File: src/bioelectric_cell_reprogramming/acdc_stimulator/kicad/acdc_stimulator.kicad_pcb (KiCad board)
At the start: 4 copper layers, 0 parts

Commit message: ci: STM32 layout done and schematic annotated
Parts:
- added C1: 100n, Capacitor_SMD:C_0402_1005Metric, F.Cu at (104.7, 48.6)
- added C10: 100n, Capacitor_SMD:C_0402_1005Metric, F.Cu at (112.9, 57.5)
- added C11: 30p, Capacitor_SMD:C_0402_1005Metric, F.Cu at (118.8, 55.8)
- added C12: 100n, Capacitor_SMD:C_0402_1005Metric, F.Cu at (112.4, 53.6)
- added C13: 100n, Capacitor_SMD:C_0402_1005Metric, F.Cu at (100.8, 48.6)
- added C14: 100n, Capacitor_SMD:C_0402_1005Metric, F.Cu at (97.6, 60.1)
- added C15: 100n, Capacitor_SMD:C_0402_1005Metric, F.Cu at (108.2, 64.2)
- added C16: 22u, Capacitor_SMD:C_0805_2012Metric, F.Cu at (223.9, 36.3)
- added C17: 10n, Capacitor_SMD:C_0402_1005Metric, F.Cu at (102.7, 48.6)
- added C18: 22u, Capacitor_SMD:C_0805_2012Metric, F.Cu at (223.9, 39.4)
- added C19: 1u, Capacitor_SMD:C_0402_1005Metric, F.Cu at (102.8, 45.3)
- added C2: 100n, Capacitor_SMD:C_0402_1005Metric, F.Cu at (196.5, 37.8)
- added C20: 1u, Capacitor_SMD:C_0402_1005Metric, F.Cu at (102.8, 43.7)
- added C21: 0.1u, Capacitor_SMD:C_0402_1005Metric, F.Cu at (196.5, 41.7)
- added C22: 10u, Capacitor_SMD:C_0603_1608Metric, F.Cu at (223.7, 64.5)
- added C23: 100n, Capacitor_SMD:C_0402_1005Metric, F.Cu at (202.2, 43.7)
- added C24: 100u, Capacitor_THT:C_Disc_D7.5mm_W2.5mm_P5.00mm, F.Cu at (205.7, 36.9)
- added C25: 100u, Capacitor_THT:C_Disc_D7.5mm_W2.5mm_P5.00mm, F.Cu at (205.7, 40.9)
- added C26: 0.1u, Capacitor_SMD:C_0402_1005Metric, F.Cu at (245.1, 64.4)
- added C27: 0.1u, Capacitor_SMD:C_0402_1005Metric, F.Cu at (245.1, 62.4)
- added C28: 1n, Capacitor_SMD:C_0402_1005Metric, F.Cu at (248.0, 60.4)
- added C29: 4.7u, Capacitor_SMD:C_0603_1608Metric, F.Cu at (230.8, 54.0)
- added C3: 10u, Capacitor_SMD:CP_Elec_5x5.4, F.Cu at (217.2, 38.3)
- added C30: 4.7u, Capacitor_SMD:C_0603_1608Metric, F.Cu at (230.8, 56.5)
- added C31: 4.7u, Capacitor_SMD:C_0603_1608Metric, F.Cu at (234.8, 46.5)
- added C32: 4.7u, Capacitor_SMD:C_0603_1608Metric, F.Cu at (234.8, 49.0)
- added C33: 4.7u, Capacitor_SMD:C_0603_1608Metric, F.Cu at (234.8, 51.5)
- added C34: 4.7u, Capacitor_SMD:C_0603_1608Metric, F.Cu at (234.8, 54.0)
- added C35: 4.7u, Capacitor_SMD:C_0603_1608Metric, F.Cu at (234.8, 56.5)
- added C36: 0.1u, Capacitor_SMD:C_0402_1005Metric, F.Cu at (245.1, 60.4)
- added C37: 4.7u, Capacitor_SMD:C_0603_1608Metric, F.Cu at (238.8, 46.5)
- added C38: 47u, Capacitor_THT:CP_Radial_D10.0mm_P5.00mm, F.Cu at (232.3, 63.6)
- added C39: 0.1u, Capacitor_SMD:C_0402_1005Metric, F.Cu at (242.2, 64.4)
- added C4: 100n, Capacitor_SMD:C_0402_1005Metric, F.Cu at (196.5, 39.8)
- added C40: 2.2u, Capacitor_SMD:C_0603_1608Metric, F.Cu at (230.8, 46.5)
- added C41: 100p, Capacitor_SMD:C_0402_1005Metric, F.Cu at (248.0, 62.4)
- added C42: 0.1u, Capacitor_SMD:C_0402_1005Metric, F.Cu at (242.2, 62.4)
- added C43: 2.2u, Capacitor_SMD:C_0603_1608Metric, F.Cu at (230.8, 49.0)
- added C44: 0.1u, Capacitor_SMD:C_0402_1005Metric, F.Cu at (242.2, 60.4)
- added C45: 15n, Capacitor_SMD:C_0402_1005Metric, F.Cu at (248.0, 64.4)
- added C46: 4.7u, Capacitor_SMD:C_0603_1608Metric, F.Cu at (230.8, 51.5)
- added C47: 1u, Capacitor_SMD:C_0402_1005Metric, F.Cu at (238.7, 110.6)
- added C48: 100n, Capacitor_SMD:C_0402_1005Metric, F.Cu at (238.7, 112.6)
- added C49: 100n, Capacitor_SMD:C_0402_1005Metric, F.Cu at (238.7, 118.5)
- added C5: 1u, Capacitor_SMD:C_0402_1005Metric, F.Cu at (104.7, 47.5)
- added C50: 47n, Capacitor_SMD:C_0402_1005Metric, F.Cu at (238.7, 114.6)
- added C51: 1u, Capacitor_SMD:C_0402_1005Metric, F.Cu at (238.7, 116.5)
- added C52: 10u, Capacitor_SMD:CP_Elec_5x5.4, F.Cu at (229.9, 125.3)
- added C53: 2.2u, Capacitor_SMD:C_0603_1608Metric, F.Cu at (243.9, 103.9)
- added C54: 47u, Capacitor_SMD:C_0805_2012Metric, F.Cu at (244.1, 101.1)
- added C55: 2.2u, Capacitor_SMD:C_0603_1608Metric, F.Cu at (218.3, 103.9)
- added C56: 47u, Capacitor_SMD:C_0805_2012Metric, F.Cu at (218.5, 101.1)
- added C57: 2.2u, Capacitor_SMD:C_0603_1608Metric, F.Cu at (218.3, 126.0)
- added C58: 47u, Capacitor_SMD:C_0805_2012Metric, F.Cu at (218.5, 123.2)
- added C6: 10n, Capacitor_SMD:C_0402_1005Metric, F.Cu at (196.5, 35.8)
- added C7: 30p, Capacitor_SMD:C_0402_1005Metric, F.Cu at (116.4, 60.8)
- added C8: 10u, Capacitor_SMD:C_0603_1608Metric, F.Cu at (119.7, 78.4)
- added C9: 100n, Capacitor_SMD:C_0402_1005Metric, F.Cu at (112.4, 60.0)
- added D1: LED, LED_SMD:LED_0402_1005Metric, F.Cu at (181.1, 72.2)
- added D2: MBR2100, MBR2100:DIOAD1910W86L670D310, F.Cu at (227.0, 89.0)
- added D3: MBR2100, MBR2100:DIOAD1910W86L670D310, F.Cu at (201.4, 89.0)
- added D4: MBR2100, MBR2100:DIOAD1910W86L670D310, F.Cu at (201.4, 111.1)
- added F1: 500mA, Fuse:Fuse_0603_1608Metric, F.Cu at (89.0, 50.0)
- added FB1: 120R, Inductor_SMD:L_0603_1608Metric, F.Cu at (100.9, 44.5)
- added IC1: AD9833BRM-REEL7, AD9833BRM-REEL7:SOP50P490X110-10N, F.Cu at (215.6, 82.2)
- added IC2: AD5122BCPZ10-RL7, AD5122BCPZ10-RL7:QFN50P300X300X80-17N-D, F.Cu at (224.1, 44.3)
- added IC3: LTC3896EFE#PBF, LTC3896EFE#PBF:SOP50P640X120-39N, F.Cu at (254.8, 50.9)
- added IC4: LTC3637IMSE#PBF, LTC3637IMSE#PBF:LTC3637IMSEPBF, F.Cu at (245.4, 95.5)
- added IC5: LTC3637IMSE#PBF, LTC3637IMSE#PBF:LTC3637IMSEPBF, F.Cu at (219.9, 95.5)
- added IC6: LTC3637IMSE#PBF, LTC3637IMSE#PBF:LTC3637IMSEPBF, F.Cu at (219.9, 117.6)
- added J1: Screw_Terminal_01x02, TerminalBlock:TerminalBlock_Altech_AK300-2_P5.00mm, F.Cu at (186.2, 41.8)
- added J2: Conn_ARM_SWD_TagConnect_TC2030-NL, Connector:Tag-Connect_TC2030-IDC-NL_2x03_P1.27mm_Vertical, F.Cu at (90.6, 63.7)
- added J3: USB_C_Receptacle_USB2.0_14P, Connector_USB:USB_C_Receptacle_GCT_USB4105-xx-A_16P_TopMnt_Horizontal, F.Cu at (82.5, 53.2)
- added J4: S4B-PH-SM4-TB, male_socket_S4B-PH-SM4-TB.pretty:CONN4_S4B-PH-SM4-TB_JST, F.Cu at (193.2, 67.2)
- added J5: IPL1-102-01-L-S-K, 1x02_socket_IPL1-102-01-L-S-K.pretty:CONN_IPL1-102-01-L-S-K_SAI, F.Cu at (173.7, 70.3)
- added J6: Screw_Terminal_01x02, TerminalBlock:TerminalBlock_Altech_AK300-2_P5.00mm, F.Cu at (173.9, 41.8)
- added J7: IPL1-102-01-L-S-K, 1x02_socket_IPL1-102-01-L-S-K.pretty:CONN_IPL1-102-01-L-S-K_SAI, F.Cu at (173.7, 78.1)
- added J8: 6620XX11122_66200211122, 1x02_socket_66200211122.pretty:66200211122, F.Cu at (231.3, 112.4)
- added J9: 6620XX11122_66200211122, 1x02_socket_66200211122.pretty:66200211122, F.Cu at (231.3, 118.6)
- added L1: 2.5, Inductor_THT:L_Radial_D7.0mm_P3.00mm, F.Cu at (206.1, 70.2)
- added L2: 2.5, Inductor_THT:L_Radial_D7.0mm_P3.00mm, F.Cu at (206.1, 53.1)
- added L3: 2.5, Inductor_THT:L_Radial_D7.0mm_P3.00mm, F.Cu at (206.1, 61.6)
- added L4: SRR0745HA-470M, SRR0745HA-470M:SRR0745HA470M, F.Cu at (251.1, 40.0)
- added L5: 10u, SRP1270-100M:INDPM137137X700N, F.Cu at (233.6, 99.0)
- added L6: 10u, SRP1270-100M:INDPM137137X700N, F.Cu at (208.1, 99.0)
- added L7: 10u, SRP1270-100M:INDPM137137X700N, F.Cu at (208.1, 121.2)
- added MOSFET1: BSZ070N08LS5ATMA1, BSZ070N08LS5ATMA1:TSDSON-8-FL_INF, F.Cu at (242.9, 112.2)
- added Q1: BSZ096N10LS5ATMA1, BSZ096N10LS5ATMA1:BSZ060NE2LS, F.Cu at (207.1, 77.7)
- added Q10: BSZ096N10LS5ATMA1, BSZ096N10LS5ATMA1:BSZ060NE2LS, F.Cu at (193.7, 89.8)
- added Q11: BSZ096N10LS5ATMA1, BSZ096N10LS5ATMA1:BSZ060NE2LS, F.Cu at (193.7, 109.0)
- added Q2: NDT3055L, Package_TO_SOT_SMD:SOT-223-3_TabPin2, F.Cu at (216.8, 67.5)
- added Q3: BSC520N15NS3G, BSC520N15NS3G:BSC093N04LSG, F.Cu at (233.0, 39.7)
- added Q4: BSC520N15NS3G, BSC520N15NS3G:BSC093N04LSG, F.Cu at (241.4, 39.7)
- added Q5: IPD320N20N3GATMA1, IPD320N20N3GATMA1:BTS3035TFATMA1, F.Cu at (245.6, 46.8)
- added Q6: BSZ096N10LS5ATMA1, BSZ096N10LS5ATMA1:BSZ060NE2LS, F.Cu at (193.7, 102.6)
- added Q7: BSZ096N10LS5ATMA1, BSZ096N10LS5ATMA1:BSZ060NE2LS, F.Cu at (193.7, 96.2)
- added Q8: IPB320P10LMATMA1, IPB320P10LMATMA1:IPB320P10LMATMA1, F.Cu at (177.7, 107.4)
- added Q9: IPB320P10LMATMA1, IPB320P10LMATMA1:IPB320P10LMATMA1, F.Cu at (177.7, 93.5)
- added R1: 10k, Resistor_SMD:R_0402_1005Metric, F.Cu at (103.4, 64.6)
- added R10: 1.8M, Resistor_SMD:R_0805_2012Metric, F.Cu at (200.1, 77.7)
- added R11: 10k, Resistor_SMD:R_0402_1005Metric, F.Cu at (214.2, 42.7)
- added R12: 10k, Resistor_SMD:R_0402_1005Metric, F.Cu at (217.1, 42.7)
- added R13: 100k, Resistor_SMD:R_0603_1608Metric, F.Cu at (223.7, 74.6)
- added R14: 172k, Resistor_SMD:R_0603_1608Metric, F.Cu at (223.7, 77.1)
- added R15: 10k, Resistor_SMD:R_0402_1005Metric, F.Cu at (214.2, 44.7)
- added R16: 10m, Resistor_SMD:R_0402_1005Metric, F.Cu at (250.9, 60.5)
- added R17: 100k, Resistor_SMD:R_0603_1608Metric, F.Cu at (238.8, 49.0)
- added R18: 301k, Resistor_SMD:R_0603_1608Metric, F.Cu at (238.8, 51.5)
- added R19: 10k, Resistor_SMD:R_0402_1005Metric, F.Cu at (250.9, 62.4)
- added R2: 10k, Resistor_SMD:R_0402_1005Metric, F.Cu at (105.5, 64.6)
- added R20: 740k, Resistor_SMD:R_0603_1608Metric, F.Cu at (238.8, 54.0)
- added R21: 4.99k, Resistor_SMD:R_0402_1005Metric, F.Cu at (250.9, 64.4)
- added R22: 10k, Resistor_SMD:R_0402_1005Metric, F.Cu at (191.3, 113.2)
- added R23: 10k, Resistor_SMD:R_0402_1005Metric, F.Cu at (191.3, 115.2)
- added R24: 10k, Resistor_SMD:R_0201_0603Metric, F.Cu at (235.6, 122.8)
- added R25: 1k, Resistor_SMD:R_0201_0603Metric, F.Cu at (235.6, 124.5)
- added R26: 1.5k, Resistor_SMD:R_0201_0603Metric, F.Cu at (235.6, 126.3)
- added R27: 1.5k, Resistor_SMD:R_0201_0603Metric, F.Cu at (235.6, 128.0)
- added R28: 200k, Resistor_SMD:R_0603_1608Metric, F.Cu at (243.9, 106.4)
- added R29: 35.7k, Resistor_SMD:R_0402_1005Metric, F.Cu at (247.3, 103.6)
- added R3: 10k, Resistor_SMD:R_0402_1005Metric, F.Cu at (105.4, 67.6)
- added R30: 42.5k, Resistor_SMD:R_0402_1005Metric, F.Cu at (221.8, 103.6)
- added R31: 10k, Resistor_SMD:R_0402_1005Metric, F.Cu at (221.8, 105.6)
- added R32: 31.25k, Resistor_SMD:R_0402_1005Metric, F.Cu at (221.8, 125.7)
- added R33: 10k, Resistor_SMD:R_0402_1005Metric, F.Cu at (221.8, 127.7)
- added R4: 1k, Resistor_SMD:R_0402_1005Metric, F.Cu at (214.2, 46.7)
- added R5: 5.1k, Resistor_SMD:R_0603_1608Metric, F.Cu at (89.0, 51.6)
- added R6: 5.1k, Resistor_SMD:R_0603_1608Metric, F.Cu at (89.0, 56.8)
- added R7: 10k, Resistor_SMD:R_0402_1005Metric, F.Cu at (217.1, 44.7)
- added R8: 10k, Resistor_SMD:R_0402_1005Metric, F.Cu at (217.1, 46.7)
- added R9: 1M, Resistor_SMD:R_0805_2012Metric, F.Cu at (200.1, 74.7)
- added SW1: SW_Push, Button_Switch_SMD:SW_Push_1P1T_NO_CK_KMR2, F.Cu at (90.4, 71.0)
- added SW2: SW_SPDT, Button_Switch_SMD:SW_SPDT_PCM12, F.Cu at (104.0, 71.7)
- added U1: STM32G473RCTx, Package_QFP:LQFP-64_10x10mm_P0.5mm, F.Cu at (105.0, 56.8)
- added U2: AMS1117-3.3, Package_TO_SOT_SMD:SOT-223-3_TabPin2, F.Cu at (216.8, 75.8)
- added U3: USBLC6-2SC6, Package_TO_SOT_SMD:SOT-23-6, F.Cu at (89.6, 54.2)
- added U4: LTC6090CFE-PBF, LTC6090CFE_PBF:TSSOP-16_FE&slash_BA_LIT, F.Cu at (152.4, 89.5)
- added U4: LTC6090CFE-PBF, LTC6090CFE_PBF:TSSOP-16_FE&slash_BA_LIT, F.Cu at (252.9, 113.0)
- added U5: LTC6090CFE-PBF, LTC6090CFE_PBF:TSSOP-16_FE&slash_BA_LIT, F.Cu at (175.0, 121.5)
- added U6: LTC6090CFE-PBF, LTC6090CFE_PBF:TSSOP-16_FE&slash_BA_LIT, F.Cu at (252.9, 121.8)
- added U7: DRV8873HPWPR, DRV8873HPWPR.pretty:PWP24_TEX, F.Cu at (241.9, 124.3)
- added Y1: 16Mhz, Crystal:Crystal_SMD_3225-4Pin_3.2x2.5mm, F.Cu at (117.6, 58.3)

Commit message: ci: layout done
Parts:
- removed the U4 at (252.9, 113.0)
- moved Q4 188.5 mm to (110.3, 175.1), turned to 90 degrees
- moved L4 183.0 mm to (120.6, 168.3), turned to 180 degrees
- moved Q5 178.4 mm to (107.0, 159.0), turned to 90 degrees
- moved Q3 177.0 mm to (110.3, 167.3), turned to 90 degrees
- moved C31 171.2 mm to (121.4, 174.8), turned to -90 degrees
- moved C32 171.0 mm to (118.9, 174.8), turned to -90 degrees
- moved C33 170.9 mm to (116.4, 174.8), turned to -90 degrees
- moved IC3 167.6 mm to (126.1, 158.3), turned to 180 degrees
- moved C44 164.4 mm to (106.9, 153.7)
- moved C37 163.9 mm to (127.4, 166.8)
- moved C39 160.9 mm to (106.9, 151.4)
- moved C42 160.9 mm to (106.9, 149.4)
- moved C29 159.4 mm to (126.7, 174.8), turned to -90 degrees
- moved C30 159.2 mm to (124.2, 174.8), turned to -90 degrees
- moved C27 158.9 mm to (121.6, 162.4), turned to -90 degrees
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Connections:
- D2 pad 1: +60V -> Net-(D2-K)
- D3 pad 1: +60V -> Net-(D3-K)
- D4 pad 1: +60V -> Net-(D4-K)
- IC4 pad 1: +60V -> Net-(D2-K)
- IC5 pad 1: +60V -> Net-(D3-K)
- IC6 pad 1: +60V -> Net-(D4-K)
- L5 pad 1: +60V -> Net-(D2-K)
- L6 pad 1: +60V -> Net-(D3-K)
- L7 pad 1: +60V -> Net-(D4-K)
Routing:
- net GND: track 0.00 -> 13.1 mm, vias 0 -> 14
- added copper zone on In1.Cu, net GND

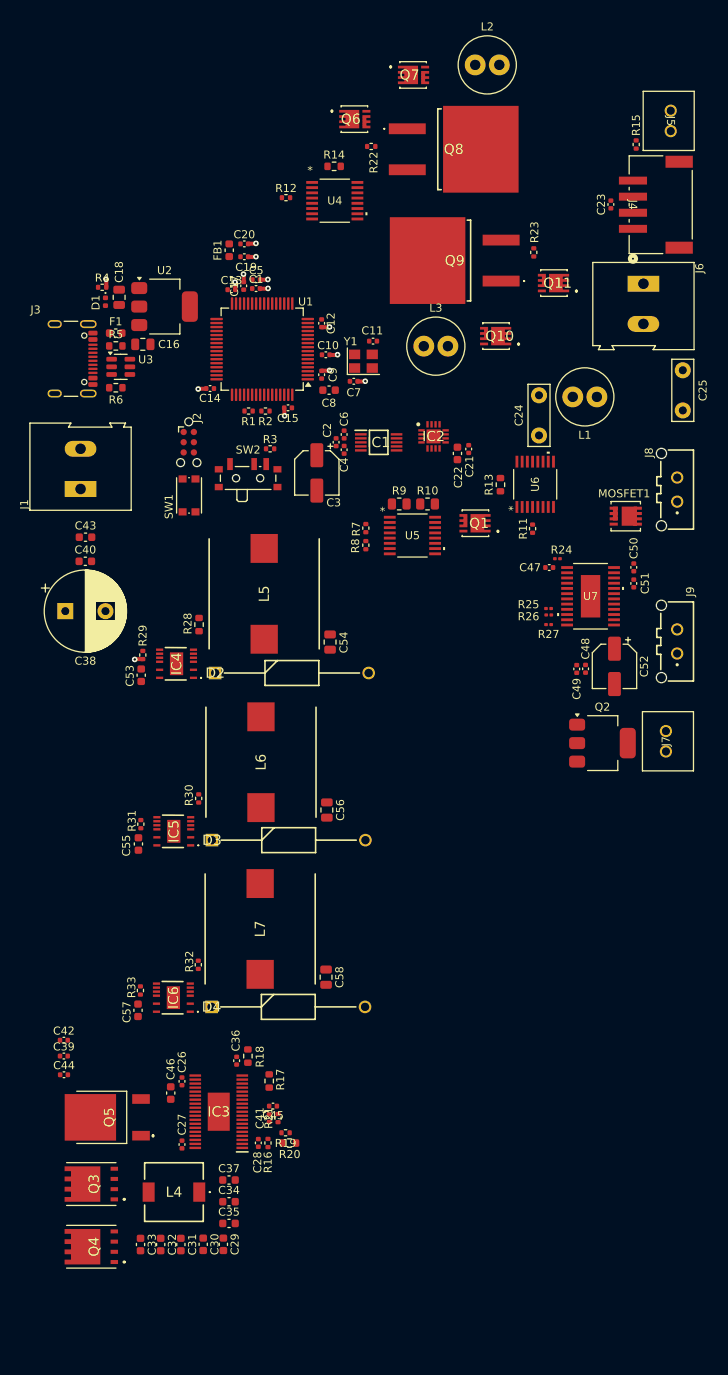
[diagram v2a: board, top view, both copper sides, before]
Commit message: GND vias added
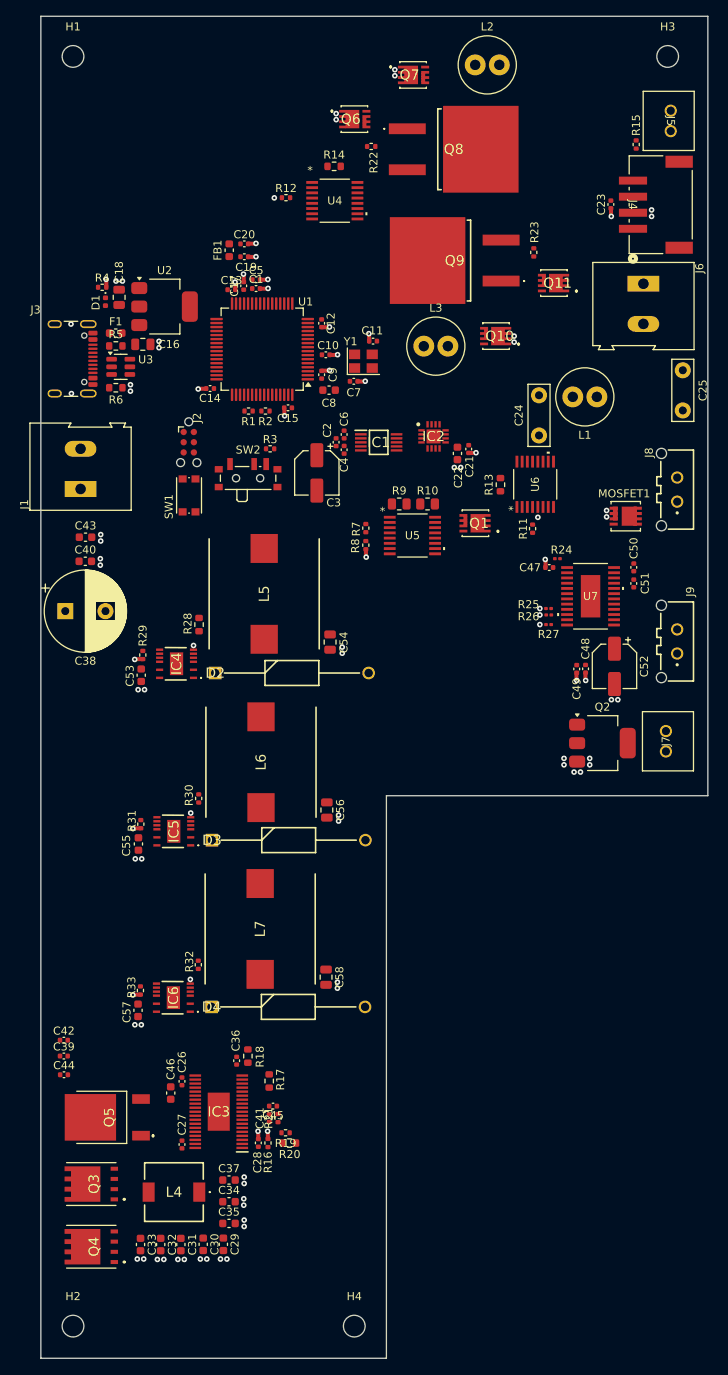
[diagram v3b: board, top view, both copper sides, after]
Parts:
- added H1: MountingHole, MountingHole:MountingHole_2.7mm_M2.5, F.Cu at (108.0, 27.0)
- added H2: MountingHole, MountingHole:MountingHole_2.7mm_M2.5, F.Cu at (108.0, 185.0)
- added H3: MountingHole, MountingHole:MountingHole_2.7mm_M2.5, F.Cu at (182.0, 27.0)
- added H4: MountingHole, MountingHole:MountingHole_2.7mm_M2.5, F.Cu at (143.0, 185.0)
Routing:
- net GND: track 13.1 -> 23.9 mm, vias 14 -> 101
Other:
- board outline added: 83 x 167 mm

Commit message: ci: adding LTspice files
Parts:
- R11: value 10k -> 1k
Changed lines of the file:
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@@
 			)
 		)
-		(property "Value" "10k"
+		(property "Value" "1k"
 			(at 0 1.17 90)
 			(layer "F.Fab")

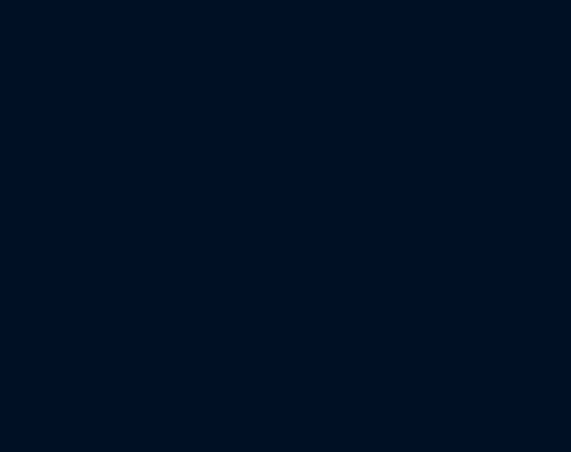
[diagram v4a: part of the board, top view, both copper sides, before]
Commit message: fix: replaced op amp with voltage divider for ADC
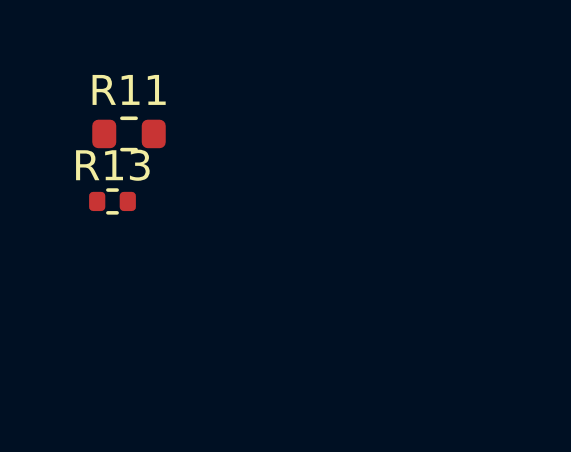
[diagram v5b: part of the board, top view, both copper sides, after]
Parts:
- added R11: 1M, Resistor_SMD:R_0603_1608Metric, F.Cu at (1.50, 0.76)
- added R13: 10k, Resistor_SMD:R_0402_1005Metric, F.Cu at (0.95, 3.00)
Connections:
- C24 pad 1: /LTC6090_FB/OUT -> Net-(C24-Pad1)

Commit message: layout finalized
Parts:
- removed the R11 at (165.2, 85.8)
- removed the R13 at (161.2, 80.3)
- removed U6: LTC6090CFE-PBF, LTC6090CFE_PBF:TSSOP-16_FE&slash_BA_LIT
- moved H4 186.4 mm to (31.0, 36.0)
- moved R11 175.3 mm to (157.2, 81.4), turned to 180 degrees
- moved R13 172.5 mm to (156.3, 77.9), turned to -90 degrees
- moved H2 171.0 mm to (24.0, 36.0)
- moved H3 158.0 mm to (24.0, 28.0)
- moved C26 123.1 mm to (185.2, 49.1)
- moved C28 123.1 mm to (194.7, 56.8)
- moved C29 123.1 mm to (190.4, 69.4)
- moved C32 123.1 mm to (182.6, 69.4)
- moved C33 123.1 mm to (180.1, 69.4)
- moved C35 123.1 mm to (191.1, 66.8)
- moved C37 123.1 mm to (191.1, 61.4)
- moved C44 123.1 mm to (170.5, 48.3)
- moved L4 123.1 mm to (184.2, 62.9)
- moved Q3 123.1 mm to (173.9, 61.9)
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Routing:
- net /USB_D-: track 0.00 -> 14.3 mm
- net /USB_D+: track 0.00 -> 14.2 mm
- net /SWCLK: track 0.00 -> 6.78 mm
- net /HSE_IN: track 0.00 -> 6.07 mm
- net /SWDIO: track 0.00 -> 5.31 mm
- net GND: track 23.9 -> 28.4 mm, vias 101 -> 100
- net /VREF: track 0.00 -> 3.18 mm
- net +3.3V: track 0.00 -> 1.95 mm
- net /HSE_OUT: track 0.00 -> 1.89 mm
- net +3.3VA: track 0.00 -> 1.75 mm
- removed copper zone on In1.Cu, net GND
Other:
- board outline removed

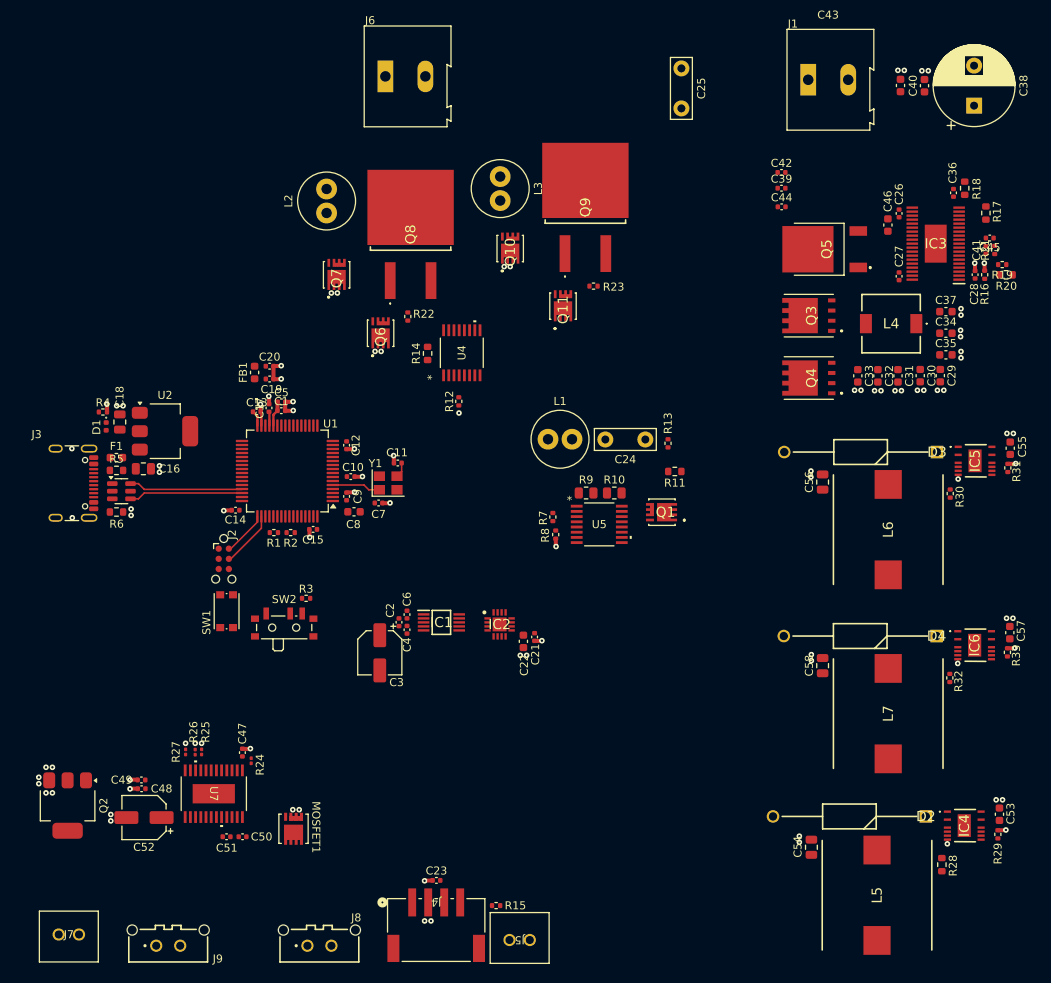
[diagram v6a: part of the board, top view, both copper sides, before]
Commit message: finished routing power supplies
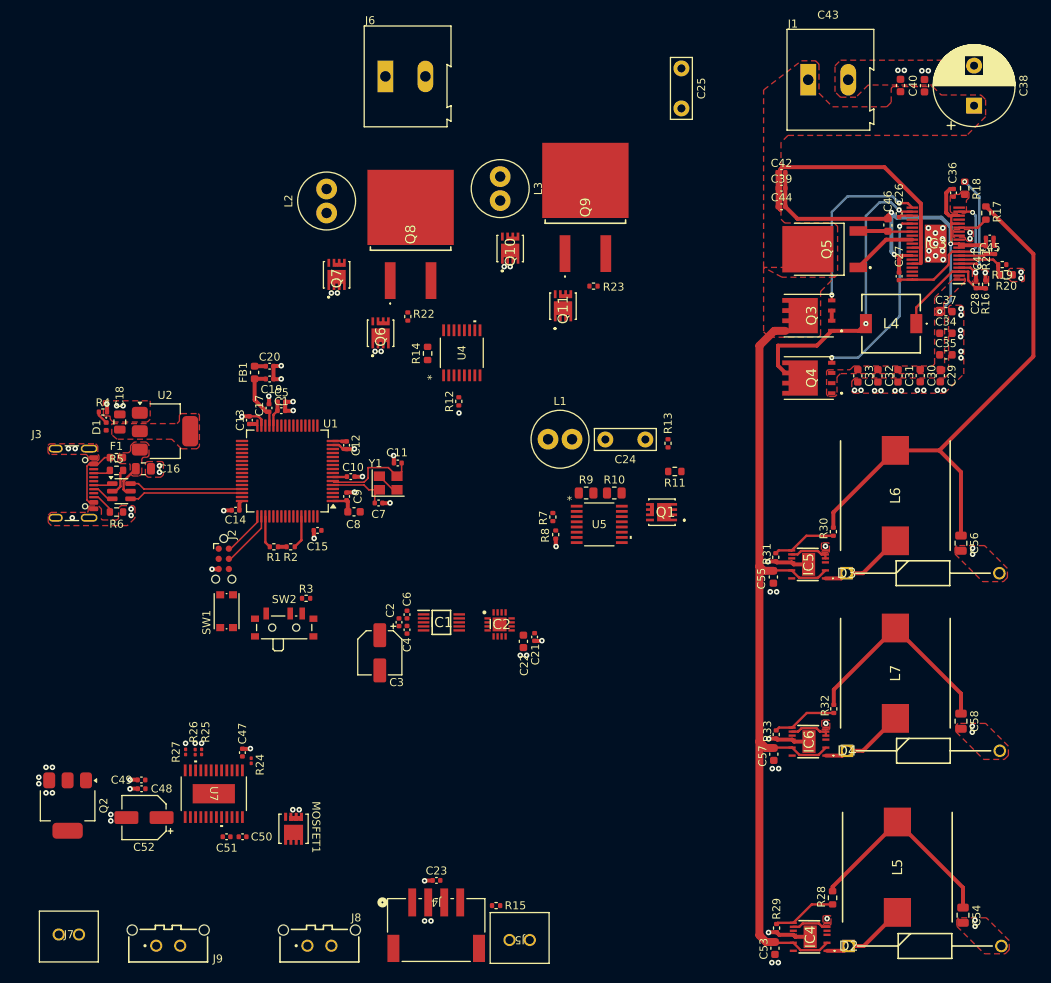
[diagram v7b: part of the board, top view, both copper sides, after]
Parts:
- moved C55 33.7 mm to (169.5, 94.6), turned to -90 degrees
- moved C57 33.2 mm to (169.6, 116.7), turned to -90 degrees
- moved C53 32.7 mm to (169.7, 141.0), turned to -90 degrees
- moved R31 31.1 mm to (169.8, 92.1), turned to -90 degrees
- moved R33 30.7 mm to (169.8, 114.3), turned to -90 degrees
- moved R29 30.0 mm to (169.9, 138.5), turned to -90 degrees
- moved IC5 24.5 mm to (173.9, 93.0), turned to 90 degrees
- moved IC6 24.0 mm to (173.9, 115.2), turned to 90 degrees
- moved IC4 23.8 mm to (174.1, 139.6), turned to 90 degrees
- moved C54 20.8 mm to (193.2, 136.8), turned to -90 degrees
- moved C56 18.9 mm to (192.9, 90.3), turned to -90 degrees
- moved D3 18.9 mm to (178.6, 94.1), turned to 0 degrees
- moved D2 18.9 mm to (178.9, 140.7), turned to 0 degrees
- moved C58 18.6 mm to (192.9, 112.6), turned to -90 degrees
- moved D4 18.2 mm to (178.7, 116.3), turned to 0 degrees
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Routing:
- net +60V: track 0.00 -> 145.0 mm
- net +5V: track 0.00 -> 72.1 mm
- net -60V: track 0.00 -> 66.2 mm, vias 0 -> 4
- net /DCDC_inverter/SW: track 0.00 -> 36.4 mm, vias 0 -> 2
- net +3.3V: track 1.95 -> 36.7 mm
- net +12V: track 0.00 -> 26.1 mm
- net /DCDC_inverter/BG: track 0.00 -> 24.2 mm, vias 0 -> 2
- net /DCDC_inverter/TG: track 0.00 -> 22.5 mm, vias 0 -> 2
- net GND: track 28.4 -> 50.7 mm, vias 100 -> 117
- net /DCDC_inverter/INTVCC: track 0.00 -> 18.2 mm, vias 0 -> 2
- net /DCDC_inverter/SENSE+: track 0.00 -> 14.1 mm
- net Net-(IC3-SS): track 0.00 -> 14.0 mm, vias 0 -> 2
- net Net-(D2-K): track 0.00 -> 10.8 mm
- net Net-(D3-K): track 0.00 -> 10.7 mm
- net Net-(D4-K): track 0.00 -> 10.6 mm
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- added copper zone on F.Cu, net +3.3V
- added copper zone on F.Cu, net +5V
- added copper zone on F.Cu, net +60V
- added copper zone on F.Cu, net -60V
- added copper zone on F.Cu, net /DCDC_inverter/INTVCC
- added copper zone on F.Cu, net GND

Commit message: ci: finished routing for signal side
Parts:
- moved R13 1.01 mm to (156.3, 76.9), turned to 90 degrees
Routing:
- net +5V: track 72.1 -> 127.9 mm
- net Net-(J6-Pin_2): track 0.00 -> 52.7 mm
- net /V_AC: track 0.00 -> 52.2 mm
- net /SPI_CLK: track 0.00 -> 51.9 mm, vias 0 -> 4
- net +3.3V: track 36.7 -> 82.2 mm, vias 0 -> 2
- net /V_DC: track 0.00 -> 43.9 mm
- net /SPI_DO: track 0.00 -> 42.0 mm, vias 0 -> 4
- net /POT_CS: track 0.00 -> 41.7 mm, vias 0 -> 2
- net /SPI_DI: track 0.00 -> 38.1 mm, vias 0 -> 4
- net /POT_OUT: track 0.00 -> 36.5 mm
- net /FG_CS: track 0.00 -> 34.7 mm, vias 0 -> 2
- net /DAC_FB: track 0.00 -> 32.4 mm
- net /H_Bridge_IN2: track 0.00 -> 30.2 mm, vias 0 -> 2
- net /DAC_DC: track 0.00 -> 26.6 mm, vias 0 -> 2
- net /V_DC2: track 0.00 -> 24.8 mm
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- added copper zone on F.Cu, net +12V
- added copper zone on F.Cu, net /LTC6090_AC/OUT
